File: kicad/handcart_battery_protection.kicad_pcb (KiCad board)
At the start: 2 copper layers, 98 parts, among them J1 Bus, K1 ‎G9TB-U1ATH-E DC12‎, K2 ALQ3F12, Q1 CMPDM302PH TR, Q2 ‎BSS816NWH6327XTSA1‎, Q3 ‎BSS816NWH6327XTSA1‎, Q4 ‎BSS816NWH6327XTSA1‎, SW1 SW_Push_LED, U1 TC4428, U10 LMC6482, U11 LMC6482, U12 ST3485, U2 REF3025, U3 ATtiny1617-M, U4 LMC6482, U5 TLV9062, U6 INA2181, U7 TPS560430, U8 IRS2008S, U9 TLV3201

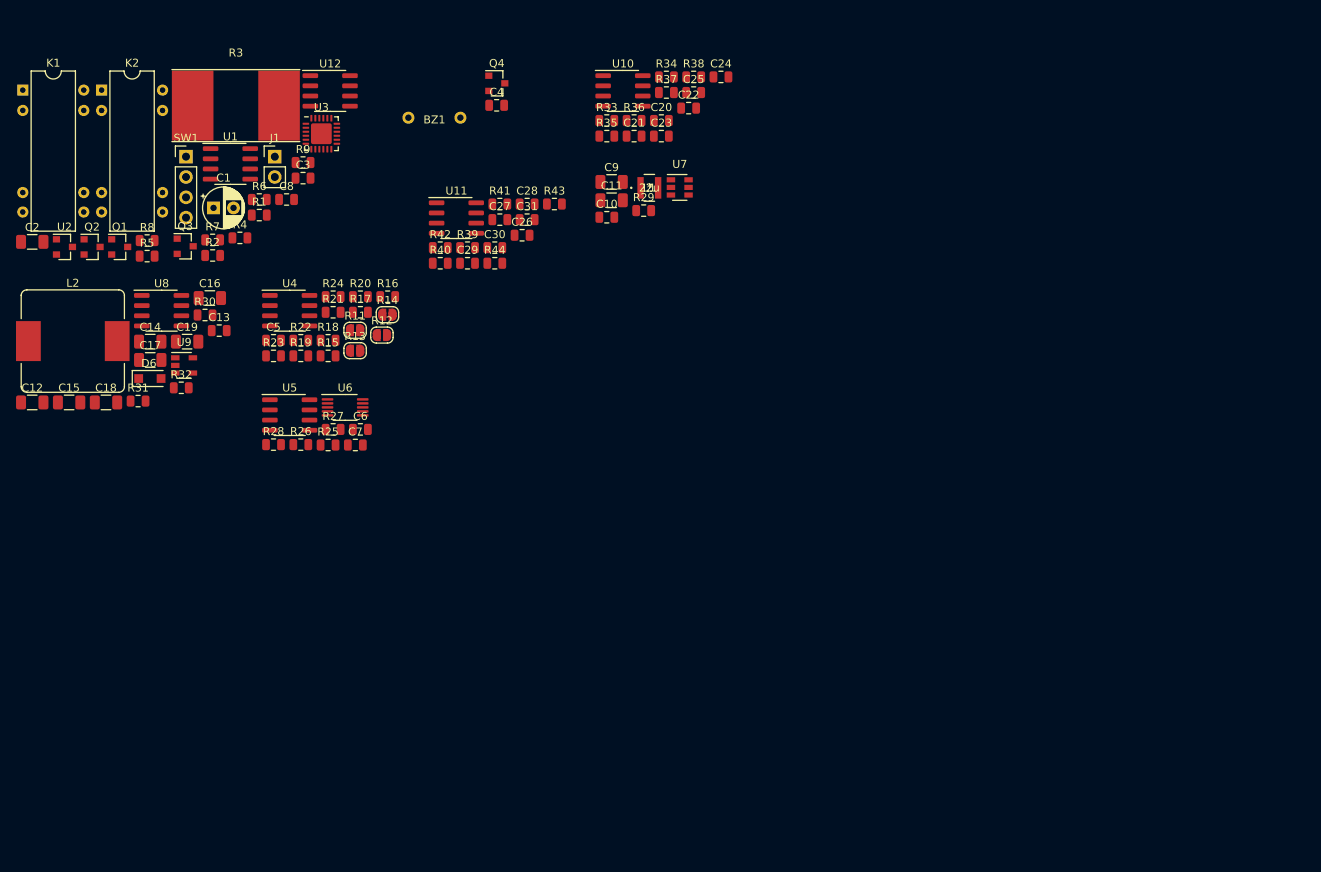
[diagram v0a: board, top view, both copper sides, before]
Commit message: Layout done. Traces only on one PCB side. Wire bridges necessary.
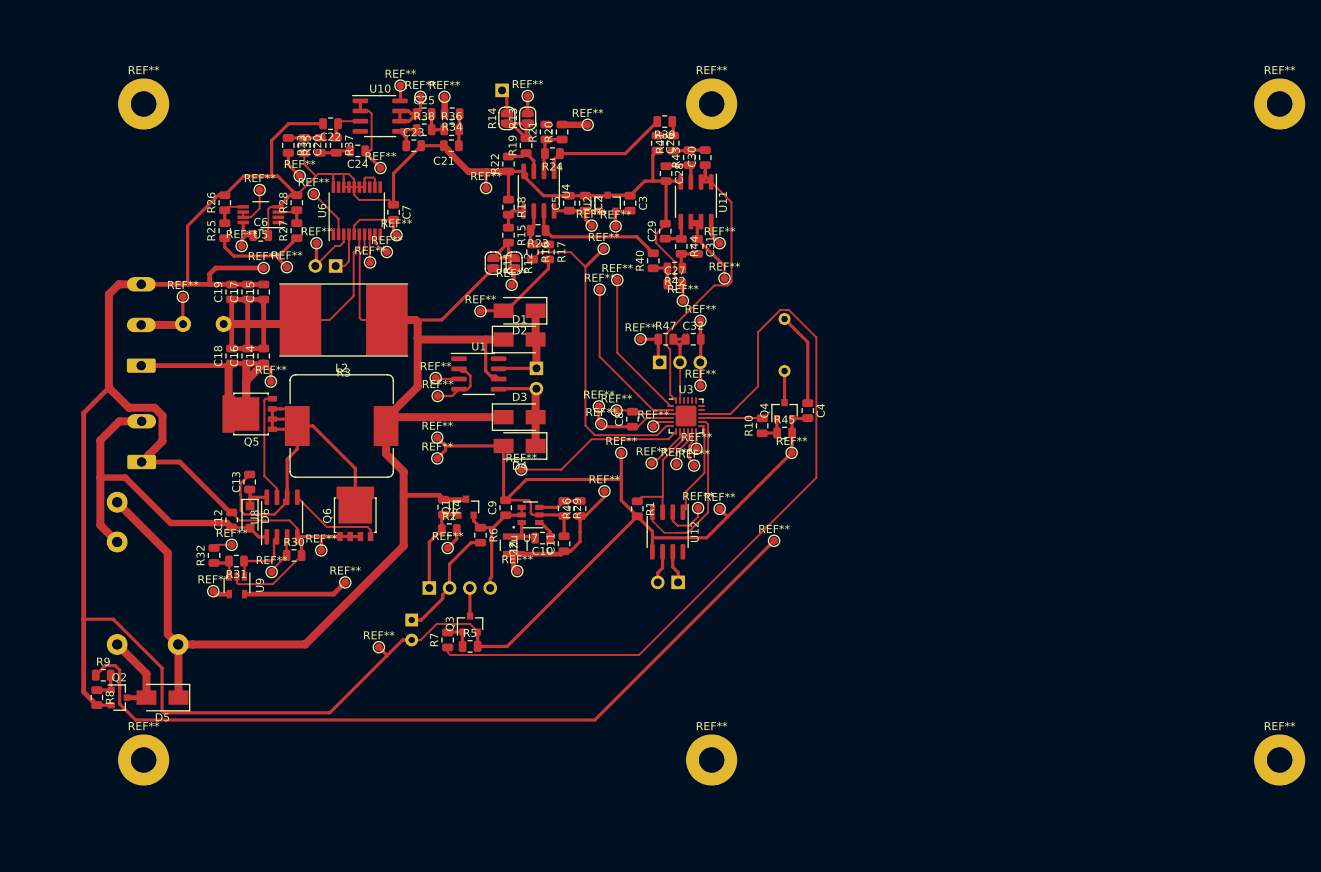
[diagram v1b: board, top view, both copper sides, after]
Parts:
- removed K1: ‎G9TB-U1ATH-E DC12‎, Relay_THT:Relay_StandexMeder_DIP_LowProfile
- added C32: 100n, Capacitor_SMD:C_0805_2012Metric, F.Cu at (117.7, 78.4)
- added D1: BAT54-7-F, Diode_SMD:D_SMA, F.Cu at (96.0, 78.4)
- added D2: BAT54-7-F, Diode_SMD:D_SMA, F.Cu at (96.0, 74.8)
- added D3: BAT54-7-F, Diode_SMD:D_SMA, F.Cu at (96.0, 88.1)
- added D4: BAT54-7-F, Diode_SMD:D_SMA, F.Cu at (96.0, 91.7)
- added D5: BAT54-7-F, Diode_SMD:D_SMA, F.Cu at (51.4, 123.2)
- added F3: Fuse 1A, Littelfuse Inc. 39211000000, Fuse:Fuse_Littelfuse_395Series, B.Cu at (59.0, 76.5)
- added J2: 100A_Shunt_In, Connector_PinSocket_2.54mm:PinSocket_1x02_P2.54mm_Vertical, B.Cu at (73.0, 69.2)
- added J3: Bat_In, Connector_Phoenix_MC_HighVoltage:PhoenixContact_MC_1,5_3-G-5.08_1x03_P5.08mm_Horizontal, B.Cu at (48.7, 81.7)
- added J4: 100A_Relay_G9TB_Coil, Connector_PinHeader_2.54mm:PinHeader_1x02_P2.54mm_Vertical, B.Cu at (98.1, 82.0)
- added J5: 100A_Relay_Out, Connector_PinHeader_2.54mm:PinHeader_1x01_P2.54mm_Vertical, B.Cu at (93.8, 47.3)
- added J6: 12V_Out, Connector_Phoenix_MC_HighVoltage:PhoenixContact_MC_1,5_2-G-5.08_1x02_P5.08mm_Horizontal, B.Cu at (48.8, 93.8)
- added J7: Program, Connector_PinHeader_2.54mm:PinHeader_1x03_P2.54mm_Vertical, B.Cu at (113.5, 81.3)
- added Q5: PSMN013-30YLC, footprints:LFPAK, F.Cu at (62.2, 87.8)
- added Q6: PSMN013-30YLC, footprints:LFPAK, F.Cu at (75.4, 100.2)
- added R10: 100, Resistor_SMD:R_0805_2012Metric, F.Cu at (126.3, 89.2)
- added R45: 100k, Resistor_SMD:R_0805_2012Metric, F.Cu at (129.1, 90.1)
- added R46: 23.7k, Resistor_SMD:R_0805_2012Metric, F.Cu at (103.6, 99.6)
- added R47: 4.7k, Resistor_SMD:R_0805_2012Metric, F.Cu at (114.3, 78.4)
- added REF**: TestPoint_Pad_D1.0mm, TestPoint:TestPoint_Pad_D1.0mm, F.Cu at (78.4, 116.9)
- added REF**: TestPoint_Pad_D1.0mm, TestPoint:TestPoint_Pad_D1.0mm, F.Cu at (97.0, 48.0)
- added REF**: TestPoint_Pad_D1.0mm, TestPoint:TestPoint_Pad_D1.0mm, F.Cu at (80.6, 65.4)
- added REF**: TestPoint_Pad_D1.0mm, TestPoint:TestPoint_Pad_D1.0mm, F.Cu at (81.1, 46.7)
- added REF**: TestPoint_Pad_D1.0mm, TestPoint:TestPoint_Pad_D1.0mm, F.Cu at (121.0, 66.4)
- added REF**: TestPoint_Pad_D1.0mm, TestPoint:TestPoint_Pad_D1.0mm, F.Cu at (111.1, 78.4)
- added REF**: TestPoint_Pad_D1.0mm, TestPoint:TestPoint_Pad_D1.0mm, F.Cu at (105.9, 86.8)
- added REF**: TestPoint_Pad_D1.0mm, TestPoint:TestPoint_Pad_D1.0mm, F.Cu at (118.6, 76.1)
- added REF**: TestPoint_Pad_D1.0mm, TestPoint:TestPoint_Pad_D1.0mm, F.Cu at (116.4, 73.6)
- added REF**: TestPoint_Pad_D1.0mm, TestPoint:TestPoint_Pad_D1.0mm, F.Cu at (91.8, 59.5)
- added REF**: TestPoint_Pad_D1.0mm, TestPoint:TestPoint_Pad_D1.0mm, F.Cu at (91.1, 74.9)
- added REF**: TestPoint_Pad_D1.0mm, TestPoint:TestPoint_Pad_D1.0mm, F.Cu at (71.2, 104.8)
- added REF**: TestPoint_Pad_D1.0mm, TestPoint:TestPoint_Pad_D1.0mm, F.Cu at (95.0, 71.6)
- added REF**: TestPoint_Pad_D1.0mm, TestPoint:TestPoint_Pad_D1.0mm, F.Cu at (66.9, 69.4)
- added REF**: TestPoint_Pad_D1.0mm, TestPoint:TestPoint_Pad_D1.0mm, F.Cu at (70.6, 66.4)
- added REF**: TestPoint_Pad_D1.0mm, TestPoint:TestPoint_Pad_D1.0mm, F.Cu at (85.7, 90.7)
- added REF**: TestPoint_Pad_D1.0mm, TestPoint:TestPoint_Pad_D1.0mm, F.Cu at (86.6, 48.1)
- added REF**: TestPoint_Pad_D1.0mm, TestPoint:TestPoint_Pad_D1.0mm, F.Cu at (77.3, 68.8)
- added REF**: TestPoint_Pad_D1.0mm, TestPoint:TestPoint_Pad_D1.0mm, F.Cu at (57.7, 109.9)
- added REF**: TestPoint_Pad_D1.0mm, TestPoint:TestPoint_Pad_D1.0mm, F.Cu at (74.2, 108.8)
- added REF**: TestPoint_Pad_D1.0mm, TestPoint:TestPoint_Pad_D1.0mm, F.Cu at (95.7, 107.4)
- added REF**: TestPoint_Pad_D1.0mm, TestPoint:TestPoint_Pad_D1.0mm, F.Cu at (96.2, 94.7)
- added REF**: TestPoint_Pad_D1.0mm, TestPoint:TestPoint_Pad_D1.0mm, F.Cu at (85.7, 93.3)
- added REF**: TestPoint_Pad_D1.0mm, TestPoint:TestPoint_Pad_D1.0mm, F.Cu at (60.0, 104.1)
- added REF**: TestPoint_Pad_D1.0mm, TestPoint:TestPoint_Pad_D1.0mm, F.Cu at (112.5, 93.9)
- added REF**: TestPoint_Pad_D1.0mm, TestPoint:TestPoint_Pad_D1.0mm, F.Cu at (87.0, 104.5)
- added REF**: TestPoint_Pad_D1.0mm, TestPoint:TestPoint_Pad_D1.0mm, F.Cu at (115.6, 94.0)
- added REF**: TestPoint_Pad_D1.0mm, TestPoint:TestPoint_Pad_D1.0mm, F.Cu at (117.8, 94.2)
- added REF**: TestPoint_Pad_D1.0mm, TestPoint:TestPoint_Pad_D1.0mm, F.Cu at (118.3, 99.5)
- added REF**: TestPoint_Pad_D1.0mm, TestPoint:TestPoint_Pad_D1.0mm, F.Cu at (121.6, 70.8)
- added REF**: TestPoint_Pad_D1.0mm, TestPoint:TestPoint_Pad_D1.0mm, F.Cu at (112.7, 89.3)
- added REF**: TestPoint_Pad_D1.0mm, TestPoint:TestPoint_Pad_D1.0mm, F.Cu at (106.6, 97.4)
- added REF**: TestPoint_Pad_D1.0mm, TestPoint:TestPoint_Pad_D1.0mm, F.Cu at (106.2, 89.0)
- added REF**: TestPoint_Pad_D1.0mm, TestPoint:TestPoint_Pad_D1.0mm, F.Cu at (121.0, 99.6)
- added REF**: TestPoint_Pad_D1.0mm, TestPoint:TestPoint_Pad_D1.0mm, F.Cu at (108.7, 92.6)
- added REF**: TestPoint_Pad_D1.0mm, TestPoint:TestPoint_Pad_D1.0mm, F.Cu at (108.1, 87.3)
- added REF**: TestPoint_Pad_D1.0mm, TestPoint:TestPoint_Pad_D1.0mm, F.Cu at (118.1, 92.1)
- added REF**: TestPoint_Pad_D1.0mm, TestPoint:TestPoint_Pad_D1.0mm, F.Cu at (83.6, 48.1)
- added REF**: TestPoint_Pad_D1.0mm, TestPoint:TestPoint_Pad_D1.0mm, F.Cu at (78.6, 57.0)
- added REF**: TestPoint_Pad_D1.0mm, TestPoint:TestPoint_Pad_D1.0mm, F.Cu at (106.0, 72.2)
- added REF**: TestPoint_Pad_D1.0mm, TestPoint:TestPoint_Pad_D1.0mm, F.Cu at (108.2, 71.0)
- added REF**: TestPoint_Pad_D1.0mm, TestPoint:TestPoint_Pad_D1.0mm, F.Cu at (105.0, 64.2)
- added REF**: TestPoint_Pad_D1.0mm, TestPoint:TestPoint_Pad_D1.0mm, F.Cu at (106.5, 67.1)
- added REF**: TestPoint_Pad_D1.0mm, TestPoint:TestPoint_Pad_D1.0mm, F.Cu at (104.5, 51.6)
- added REF**: TestPoint_Pad_D1.0mm, TestPoint:TestPoint_Pad_D1.0mm, F.Cu at (130.0, 92.6)
- added REF**: TestPoint_Pad_D1.0mm, TestPoint:TestPoint_Pad_D1.0mm, F.Cu at (70.2, 60.2)
- added REF**: TestPoint_Pad_D1.0mm, TestPoint:TestPoint_Pad_D1.0mm, F.Cu at (61.2, 66.8)
- added REF**: MountingHole_3.2mm_M3_Pad, MountingHole:MountingHole_3.2mm_M3_Pad, F.Cu at (120.0, 131.0)
- added REF**: MountingHole_3.2mm_M3_Pad, MountingHole:MountingHole_3.2mm_M3_Pad, F.Cu at (120.0, 49.0)
- added REF**: MountingHole_3.2mm_M3_Pad, MountingHole:MountingHole_3.2mm_M3_Pad, F.Cu at (191.0, 131.0)
- added REF**: MountingHole_3.2mm_M3_Pad, MountingHole:MountingHole_3.2mm_M3_Pad, F.Cu at (191.0, 49.0)
- added REF**: MountingHole_3.2mm_M3_Pad, MountingHole:MountingHole_3.2mm_M3_Pad, F.Cu at (49.0, 49.0)
- added REF**: MountingHole_3.2mm_M3_Pad, MountingHole:MountingHole_3.2mm_M3_Pad, F.Cu at (49.0, 131.0)
- added REF**: TestPoint_Pad_D1.0mm, TestPoint:TestPoint_Pad_D1.0mm, F.Cu at (63.5, 59.8)
- added REF**: TestPoint_Pad_D1.0mm, TestPoint:TestPoint_Pad_D1.0mm, F.Cu at (85.8, 85.5)
- added REF**: TestPoint_Pad_D1.0mm, TestPoint:TestPoint_Pad_D1.0mm, F.Cu at (118.6, 84.2)
- added REF**: TestPoint_Pad_D1.0mm, TestPoint:TestPoint_Pad_D1.0mm, F.Cu at (85.5, 83.2)
- added REF**: TestPoint_Pad_D1.0mm, TestPoint:TestPoint_Pad_D1.0mm, F.Cu at (127.8, 103.6)
- added REF**: TestPoint_Pad_D1.0mm, TestPoint:TestPoint_Pad_D1.0mm, F.Cu at (68.5, 58.0)
- added REF**: TestPoint_Pad_D1.0mm, TestPoint:TestPoint_Pad_D1.0mm, F.Cu at (64.0, 69.5)
- added REF**: TestPoint_Pad_D1.0mm, TestPoint:TestPoint_Pad_D1.0mm, F.Cu at (108.0, 64.3)
- added REF**: TestPoint_Pad_D1.0mm, TestPoint:TestPoint_Pad_D1.0mm, F.Cu at (65.0, 107.5)
- added REF**: TestPoint_Pad_D1.0mm, TestPoint:TestPoint_Pad_D1.0mm, F.Cu at (79.4, 67.5)
- added REF**: TestPoint_Pad_D1.0mm, TestPoint:TestPoint_Pad_D1.0mm, F.Cu at (53.9, 73.1)
- added REF**: TestPoint_Pad_D1.0mm, TestPoint:TestPoint_Pad_D1.0mm, F.Cu at (64.9, 83.7)
- BZ1, C1, J1, SW1: moved to B.Cu
- C11, C12, C14, C15, C16, C17, C18, C19, C2, C9: footprint Capacitor_SMD:C_1206_3216Metric -> Capacitor_SMD:C_0805_2012Metric
- K2: footprint Relay_THT:Relay_StandexMeder_DIP_LowProfile -> footprints:ALQ3F12; moved to B.Cu
- R1: value 100u -> 100k
- R32: value 6.49k -> 6.8k
- U5: footprint Package_SO:SOIC-8_3.9x4.9mm_P1.27mm -> Package_SO:VSSOP-8_3.0x3.0mm_P0.65mm
- U6: value INA2181 -> INA4181; footprint Package_SO:VSSOP-10_3x3mm_P0.5mm -> Package_SO:TSSOP-20_4.4x6.5mm_P0.65mm
- moved J1 73.3 mm to (115.8, 108.8), turned to 90 degrees
- moved K2 71.3 mm to (54.5, 117.8), turned to 90 degrees
- moved U12 69.4 mm to (114.5, 102.5), turned to 270 degrees
- moved C2 69.3 mm to (104.2, 61.4), turned to 270 degrees
- moved R9 68.8 mm to (44.0, 120.4)
- moved U2 68.1 mm to (107.0, 61.4), turned to 90 degrees
- moved R5 63.3 mm to (89.8, 116.8)
- moved SW1 61.9 mm to (84.7, 109.5), turned to 270 degrees
- moved R1 59.8 mm to (110.7, 99.6), turned to 270 degrees
- moved Q3 59.1 mm to (89.8, 114.0), turned to 90 degrees
- moved R7 58.0 mm to (87.0, 116.0), turned to 90 degrees
- moved U3 57.6 mm to (116.8, 88.0)
- moved R8 57.5 mm to (43.1, 123.2), turned to 270 degrees
- moved C1 57.2 mm to (82.5, 113.5), turned to 270 degrees
- moved Q2 56.4 mm to (46.0, 123.2)
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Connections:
- C14 pad 1: (no net) -> /24V_Bat
- C14 pad 2: (no net) -> /12V_Bat
- C15 pad 1: (no net) -> /12V_Bat
- C15 pad 2: (no net) -> GND
- C16 pad 1: (no net) -> /24V_Bat
- C16 pad 2: (no net) -> /12V_Bat
- C17 pad 1: (no net) -> /12V_Bat
- C17 pad 2: (no net) -> GND
- C18 pad 1: (no net) -> /24V_Bat
- C18 pad 2: (no net) -> /12V_Bat
- C19 pad 1: (no net) -> /12V_Bat
- C19 pad 2: (no net) -> GND
- C6 pad 1: +5V -> +3V3
- C7 pad 2: +5V -> +3V3
- L2 pad 2: /12V_switchable -> /12V_rail
- Q4 pad 1: /buzzer_pwm -> Net-(Q4-Pad1)
- R1 pad 1: /100A_sense_H -> /TX_EN
- R1 pad 2: /100A_sense_L -> GND
- R12 pad 2: /12V_switchable -> /100A_sense_L
- R13 pad 2: (no net) -> /24V_Bat
- R14 pad 2: (no net) -> /24V_switchable
- R23 pad 1: /voltage_monitor/24V_sense -> /voltage_monitor/12V_sense
- R24 pad 1: /voltage_monitor/12V_sense -> /voltage_monitor/24V_sense
- R29 pad 2: +3V3 -> GND
- R3 pad 1: /5A_sense_L -> /12V_rail
- R3 pad 2: /100A_sense_L -> /12V_Bat
- U3 pad 23: (no net) -> /~RESET~_UPDI
- U4 pad 1: /voltage_monitor/12V_sense -> /voltage_monitor/24V_sense
- U4 pad 7: /voltage_monitor/24V_sense -> /voltage_monitor/12V_sense
- U5 pad 8: +5V -> +3V3
- U6 pad 1: /current_monitor/100A_sense -> (no net)
- U6 pad 10: +5V -> (no net)
- U6 pad 2: /100A_sense_L -> /current_monitor/100A_sense
- U6 pad 3: /100A_sense_H -> /100A_sense_L
- U6 pad 4: GND -> /100A_sense_H
- U6 pad 5: /current_monitor/0.3V -> +3V3
- U6 pad 6: Net-(U5-Pad6) -> /12V_Bat
- U6 pad 7: /100A_sense_L -> /12V_rail
- U6 pad 8: /5A_sense_L -> /5A_sense_unfiltered
- U6 pad 9: /5A_sense_unfiltered -> Net-(U5-Pad6)
- U8 pad 5: (no net) -> Net-(Q6-Pad2)
- U8 pad 7: (no net) -> Net-(Q5-Pad2)
- U9 pad 4: /5A_sense -> /5A_sense_unfiltered
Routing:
- net GND: track 0.00 -> 507.4 mm
- net /12V_rail: track 0.00 -> 165.6 mm
- net /12V_relay_ctrl: track 0.00 -> 102.0 mm
- net /LED: track 0.00 -> 98.7 mm
- net +3V3: track 0.00 -> 74.9 mm
- net +2V5: track 0.00 -> 62.8 mm
- net /12V_Bat: track 0.00 -> 55.5 mm
- net Net-(C13-Pad2): track 0.00 -> 47.2 mm
- net /12V_switchable: track 0.00 -> 43.6 mm
- net /24V_Bat: track 0.00 -> 40.3 mm
- net /24V_sense: track 0.00 -> 38.5 mm
- net /100A_sense: track 0.00 -> 31.1 mm
- net /5A_sense: track 0.00 -> 26.8 mm
- net /DAC_Balancer_Vset: track 0.00 -> 23.7 mm
- net /UART_Tx: track 0.00 -> 21.6 mm
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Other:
- net class Default: clearance 0.2 -> 0.3
- rule trace_clearance: 0.2 -> 0.3

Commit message: Added Bottom-layer-traces. Added ground plane. PCB outline shrinked to 100x100.
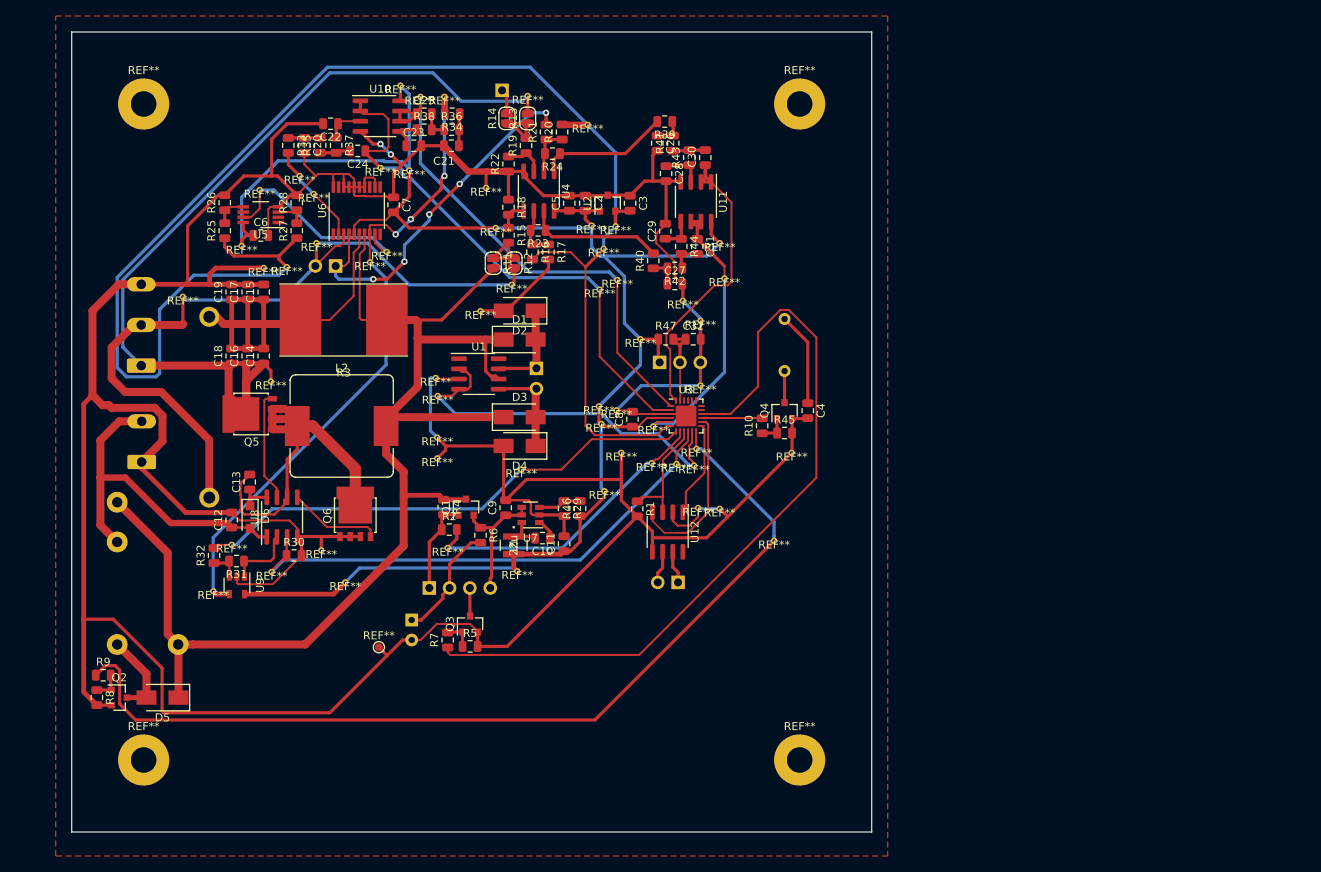
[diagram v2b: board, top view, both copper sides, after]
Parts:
- removed the REF** at (120.0, 131.0)
- removed the REF** at (191.0, 131.0)
- removed the REF** at (191.0, 49.0)
- added REF**: via, footprints:via, F.Cu at (93.0, 64.5)
- added REF**: MountingHole_3.2mm_M3_Pad, MountingHole:MountingHole_3.2mm_M3_Pad, F.Cu at (131.0, 131.0)
- F3: footprint Fuse:Fuse_Littelfuse_395Series -> footprints:Fuse_Holder
- REF** (x58): value TestPoint_Pad_D1.0mm -> via; footprint TestPoint:TestPoint_Pad_D1.0mm -> footprints:via
- moved REF** 11.0 mm to (131.0, 49.0)
- moved F3 10.6 mm to (57.2, 86.9), turned to 270 degrees
- moved REF** 8.26 mm to (82.2, 57.3)
- moved C7 0.93 mm to (80.2, 61.6)
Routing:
- net +3V3: track 74.9 -> 219.7 mm
- net +2V5: track 62.8 -> 196.3 mm
- net /100A_sense_L: track 19.7 -> 96.0 mm
- net /5A_sense_unfiltered: track 7.82 -> 83.2 mm, vias 0 -> 3
- net /24V_Bat: track 40.3 -> 115.0 mm
- net /~BAL_Shutdown: track 9.85 -> 66.0 mm
- net /DAC_Balancer_Vset: track 23.7 -> 63.8 mm
- net /100A_sense_H: track 5.30 -> 44.7 mm, vias 0 -> 5
- net /5A_sense: track 26.8 -> 65.9 mm
- net /100A_sense: track 31.1 -> 68.7 mm
- net /24V_relay_ctrl: track 12.4 -> 48.0 mm
- net GND: track 507.4 -> 541.6 mm, vias 0 -> 2
- net /~uC_EN: track 8.38 -> 38.3 mm
- net /12V_sense: track 13.4 -> 36.8 mm
- net Net-(U5-Pad6): track 8.51 -> 27.6 mm
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- added copper zone on F.Cu, net GND
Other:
- board outline added: 100 x 100 mm
